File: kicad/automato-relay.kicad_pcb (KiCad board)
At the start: 2 copper layers, 39 parts, among them J1 TE-3-213598-4, J2 Screw_Terminal_01x03, J3 TE-3-213598-4, J4 Screw_Terminal_01x05, J5 TE-3-213598-4, J6 TE-3-213598-4, J7 Screw_Terminal_01x05, J8 TE-3-213598-4, K1 G5LE-14, K2 G5LE-14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

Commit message: Final Rev
Added varistor, poured power planes, added mounting holes, modified data headers, added space for IEC connector.
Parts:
- V1: footprint Varistor:RV_Disc_D7mm_W3.5mm_P5mm -> Varistor:RV_Disc_D15.5mm_W3.9mm_P7.5mm
- moved D10 4.00 mm to (160.0, 126.0)
- moved D11 4.00 mm to (220.0, 126.0)
- moved D12 4.00 mm to (280.0, 126.0)
- moved D9 4.00 mm to (100.0, 126.0)
- moved K1 4.00 mm to (98.0, 138.0)
- moved K2 4.00 mm to (158.0, 138.0)
- moved K3 4.00 mm to (218.0, 138.0)
- moved K4 4.00 mm to (278.0, 138.0)
- moved Q1 4.00 mm to (101.0, 121.0)
- moved Q2 4.00 mm to (161.0, 121.0)
- moved Q3 4.00 mm to (221.0, 121.0)
- moved Q4 4.00 mm to (281.0, 121.0)
- moved R2 4.00 mm to (157.0, 121.0)
- moved R4 4.00 mm to (217.0, 121.0)
- moved R5 4.00 mm to (97.0, 121.0)
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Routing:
- net 3V3: track 332.4 -> 65.6 mm, vias 6 -> 3
- net GND: track 542.1 -> 290.9 mm, vias 6 -> 7
- net ACL: track 316.9 -> 70.6 mm
- net ACE: track 312.2 -> 407.1 mm, vias 0 -> 10
- net Net-(C1-Pad1): track 23.2 -> 0.00 mm
- net Net-(C4-Pad1): track 23.2 -> 0.00 mm
- net Net-(C2-Pad1): track 22.6 -> 0.00 mm
- net Net-(C3-Pad1): track 22.2 -> 0.00 mm
- net LATCH: track 346.9 -> 345.1 mm
- net CTRL1: track 26.8 -> 28.5 mm
- net SDI: track 58.6 -> 57.1 mm
- net CTRL2: track 84.3 -> 85.4 mm
- net SDO: track 271.3 -> 270.4 mm
- net CTRL4: track 209.3 -> 210.1 mm
- net CTRL3: track 147.2 -> 147.9 mm
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- added copper zone on B.Cu, net 3V3
- added copper zone on B.Cu, net ACE
- added copper zone on F.Cu, net ACE
- added copper zone on B.Cu, net ACL
- added copper zone on B.Cu, net ACN
- added copper zone on B.Cu, net GND
- added copper zone on F.Cu, net Net-(C1-Pad1)
- added copper zone on F.Cu, net Net-(C2-Pad1)
- added copper zone on F.Cu, net Net-(C3-Pad1)
- added copper zone on F.Cu, net Net-(C4-Pad1)
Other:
- board outline added: 308 x 75 mm
- net class EARTH added: clearance 1, trace_width 0.25, via_dia 0.8, via_drill 0.4
- net class HV: trace_width 6 -> 8
- board text added: "Automato Relay v0.1"

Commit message: layout: remove vias on SDO
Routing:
- net SDO: track 270.4 -> 287.5 mm, vias 3 -> 1

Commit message: layout: add Earth pour on southern half of board (both sides)
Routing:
- net ACE: track 407.1 -> 444.9 mm, vias 10 -> 4
- net SDO: track 287.5 -> 286.7 mm
- net (no net): vias 4 -> 0

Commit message: layout: add GND and 3V3 pours on northern half of board
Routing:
- net GND: track 290.9 -> 71.9 mm, vias 7 -> 0
- net 3V3: track 65.6 -> 81.1 mm, vias 3 -> 1
- added copper zone on F.Cu, net GND
- removed copper zone on B.Cu, net GND
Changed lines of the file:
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@@
     (thickness 1.6)
     (drawings 7)
-    (tracks 263)
+    (tracks 240)
     (zones 0)
     (modules 39)
@@
   )
   (setup
-    (last_trace_width 3)
+    (last_trace_width 0.4572)
     (user_trace_width 0.3048)
     (user_trace_width 0.4572)
@@
   (segment (start 280 132) (end 280 127) (width 1) (layer F.Cu) (net 12))
   (segment (start 58 110.8) (end 58.2 110.6) (width 1) (layer F.Cu) (net 12))
-  (segment (start 58 121) (end 58 110.8) (width 5) (layer F.Cu) (net 12))
   (segment (start 100 127) (end 100 131.000024) (width 1) (layer F.Cu) (net 12))
-  (segment (start 100 132) (end 100 129) (width 1) (layer B.Cu) (net 12))
   (segment (start 160 132) (end 160 129) (width 1) (layer B.Cu) (net 12))
-  (segment (start 220 132) (end 220 129) (width 1) (layer B.Cu) (net 12))
-  (segment (start 58.2 121.2) (end 58 121) (width 1) (layer B.Cu) (net 12))
-  (segment (start 58.2 121.3) (end 58.2 121.2) (width 1) (layer B.Cu) (net 12))
-  (via (at 58.2 121.3) (size 1.5) (drill 1) (layers F.Cu B.Cu) (net 12))
-  (segment (start 58.2 128.2) (end 58.2 121.3) (width 5) (layer B.Cu) (net 12))
-  (segment (start 58.5 128.5) (end 58.2 128.2) (width 5) (layer B.Cu) (net 12))
-  (via (at 78.5 127.5) (size 0.8) (drill 0.4) (layers F.Cu B.Cu) (net 12))
-  (segment (start 77.87 127.5) (end 76.445 127.575) (width 0.6096) (layer F.Cu) (net 12))
-  (segment (start 78.5 127.5) (end 77.87 127.5) (width 0.6096) (layer F.Cu) (net 12))
-  (segment (start 277 129) (end 280 132) (width 1) (layer B.Cu) (net 12))
   (segment (start 68.825 128.45) (end 68.34239 128.93261) (width 0.4572) (layer F.Cu) (net 12))
   (segment (start 68.825 127.575) (end 68.825 128.45) (width 0.4572) (layer F.Cu) (net 12))
@@
   (via (at 66.000072 128.906179) (size 0.8) (drill 0.4) (layers F.Cu B.Cu) (net 12))
   (segment (start 66.026503 128.93261) (end 66.000072 128.906179) (width 0.4572) (layer F.Cu) (net 12))
-  (segment (start 280 132) (end 280 130) (width 1.5) (layer B.Cu) (net 12))
-  (segment (start 29.36 131.32) (end 30.68 130) (width 1) (layer B.Cu) (net 12))
   (segment (start 29 131.32) (end 29.36 131.32) (width 1) (layer B.Cu) (net 12))
+  (segment (start 73.575 131.32) (end 29 131.32) (width 0.4572) (layer F.Cu) (net 12))
+  (segment (start 76.445 128.45) (end 73.575 131.32) (width 0.4572) (layer F.Cu) (net 12))
+  (segment (start 76.445 127.575) (end 76.445 128.45) (width 0.4572) (layer F.Cu) (net 12))
   (segment (start 302 115) (end 313.24 126.24) (width 1) (layer B.Cu) (net 13))
   (segment (start 40 115) (end 302 115) (width 1) (layer B.Cu) (net 13))
@@
   (segment (start 70.517461 129.788789) (end 34.805989 129.788789) (width 0.4572) (layer F.Cu) (net 13))
   (segment (start 31.2572 126.24) (end 29 126.24) (width 0.4572) (layer F.Cu) (net 13))
+  (segment (start 71.5 130.5) (end 73.905 128.095) (width 0.4572) (layer F.Cu) (net 14))
+  (segment (start 32.254198 130.5) (end 71.5 130.5) (width 0.4572) (layer F.Cu) (net 14))
+  (segment (start 30.754198 129) (end 32.254198 130.5) (width 0.4572) (layer F.Cu) (net 14))
+  (segment (start 73.905 128.095) (end 73.905 127.575) (width 0.4572) (layer F.Cu) (net 14))
+  (segment (start 27.851174 129) (end 30.754198 129) (width 0.4572) (layer F.Cu) (net 14))
+  (segment (start 26.5 127.648826) (end 27.851174 129) (width 0.4572) (layer F.Cu) (net 14))
+  (segment (start 26.5 123.66) (end 26.5 127.648826) (width 0.4572) (layer F.Cu) (net 14))
   (segment (start 29 121.16) (end 26.5 123.66) (width 0.4572) (layer F.Cu) (net 14))
-  (segment (start 26.5 123.66) (end 26.5 126.797653) (width 0.4572) (layer F.Cu) (net 14))
-  (segment (start 29.754198 128) (end 32.254198 130.5) (width 0.4572) (layer F.Cu) (net 14))
-  (segment (start 26.5 126.797653) (end 27.702347 128) (width 0.4572) (layer F.Cu) (net 14))
-  (segment (start 27.702347 128) (end 29.754198 128) (width 0.4572) (layer F.Cu) (net 14))
-  (segment (start 32.254198 130.5) (end 71.5 130.5) (width 0.4572) (layer F.Cu) (net 14))
-  (segment (start 71.5 130.5) (end 73.905 128.095) (width 0.4572) (layer F.Cu) (net 14))
-  (segment (start 73.905 128.095) (end 73.905 127.575) (width 0.4572) (layer F.Cu) (net 14))
   (segment (start 29 116.08) (end 30.92 116.08) (width 1) (layer B.Cu) (net 15))
   (segment (start 316.24 113) (end 319 115.76) (width 1) (layer B.Cu) (net 15))
@@
   (segment (start 279.9625 121.9125) (end 280 121.95) (width 1) (layer F.Cu) (net 16))
   (segment (start 277 121.9125) (end 279.9625 121.9125) (width 1) (layer F.Cu) (net 16))
-  (via (at 214 123) (size 0.8) (drill 0.4) (layers F.Cu B.Cu) (net 16))
-  (segment (start 67.555 122.425) (end 67.555 120.555) (width 0.4572) (layer F.Cu) (net 16))
   (segment (start 318.68 111) (end 319 110.68) (width 1) (layer B.Cu) (net 16))
-  (segment (start 67 111) (end 318.68 111) (width 1) (layer B.Cu) (net 16))
   (segment (start 97 121.9125) (end 96.0875 121.9125) (width 1) (layer F.Cu) (net 16))
   (segment (start 96.0875 121.9125) (end 94.75 123.25) (width 1) (layer F.Cu) (net 16))
-  (via (at 274 123) (size 0.8) (drill 0.4) (layers F.Cu B.Cu) (net 16))
-  (via (at 94.75 123.25) (size 0.8) (drill 0.4) (layers F.Cu B.Cu) (net 16))
-  (segment (start 275.0875 121.9125) (end 274 123) (width 1) (layer F.Cu) (net 16))
-  (segment (start 277 121.9125) (end 275.0875 121.9125) (width 1) (layer F.Cu) (net 16))
-  (segment (start 215.0875 121.9125) (end 214 123) (width 1) (layer F.Cu) (net 16))
-  (segment (start 217 121.9125) (end 215.0875 121.9125) (width 1) (layer F.Cu) (net 16))
-  (via (at 154 123) (size 0.8) (drill 0.4) (layers F.Cu B.Cu) (net 16))
-  (segment (start 155.0875 121.9125) (end 157 121.9125) (width 1) (layer F.Cu) (net 16))
-  (segment (start 154 123) (end 155.0875 121.9125) (width 1) (layer F.Cu) (net 16))
-  (segment (start 72.635 125.135) (end 72.635 127.575) (width 0.6096) (layer F.Cu) (net 16))
-  (segment (start 67 109.5) (end 67 109.5) (width 2) (layer F.Cu) (net 16))
-  (via (at 67 109.5) (size 1.5) (drill 1) (layers F.Cu B.Cu) (net 16))
-  (segment (start 67.5 120) (end 67.5 120) (width 2) (layer F.Cu) (net 16))
-  (segment (start 67 110.5) (end 67 119) (width 5) (layer F.Cu) (net 16))
-  (via (at 67 119.5) (size 1.5) (drill 1) (layers F.Cu B.Cu) (net 16))
-  (segment (start 67 119) (end 67 119.000032) (width 2) (layer F.Cu) (net 16))
-  (via (at 72.5 124.5) (size 0.8) (drill 0.4) (layers F.Cu B.Cu) (net 16))
-  (segment (start 72.635 124.635) (end 72.5 124.5) (width 0.6096) (layer F.Cu) (net 16))
-  (segment (start 72.635 125.135) (end 72.635 124.635) (width 0.6096) (layer F.Cu) (net 16))
+  (segment (start 32 114) (end 29 111) (width 0.4572) (layer F.Cu) (net 16))
+  (segment (start 32 119) (end 32 114) (width 0.4572) (layer F.Cu) (net 16))
+  (segment (start 38 125) (end 32 119) (width 0.4572) (layer F.Cu) (net 16))
+  (segment (start 64.98 125) (end 38 125) (width 0.4572) (layer F.Cu) (net 16))
+  (segment (start 67.555 122.425) (end 64.98 125) (width 0.4572) (layer F.Cu) (net 16))
+  (segment (start 67.555 123.3) (end 67.555 122.425) (width 0.4572) (layer F.Cu) (net 16))
+  (segment (start 69.255 125) (end 67.555 123.3) (width 0.4572) (layer F.Cu) (net 16))
+  (segment (start 70.935 125) (end 69.255 125) (width 0.4572) (layer F.Cu) (net 16))
+  (segment (start 72.635 126.7) (end 70.935 125) (width 0.4572) (layer F.Cu) (net 16))
+  (segment (start 72.635 127.575) (end 72.635 126.7) (width 0.4572) (layer F.Cu) (net 16))
   (segment (start 64.425 127.575) (end 67.555 127.575) (width 0.4572) (layer F.Cu) (net 17))
   (segment (start 64 127) (end 64.425 127.575) (width 0.4572) (layer F.Cu) (net 17))
@@
     )
   )
-  (zone (net 16) (net_name GND) (layer B.Cu) (hatch edge 0.508)
-    (connect_pads yes (clearance 0.5))
-    (min_thickness 0.254)
-    (fill yes (arc_segments 32) (thermal_gap 0.508) (thermal_bridge_width 0.508) (smoothing fillet) (radius 2))
-    (polygon
-      (pts
-        (xy 321 125) (xy 27 125) (xy 27 107) (xy 321 107)
-      )
-    )
-  )
-  (zone (net 12) (net_name 3V3) (layer B.Cu) (hatch edge 0.508)
-    (connect_pads yes (clearance 0.75))
-    (min_thickness 0.254)
-    (fill yes (arc_segments 32) (thermal_gap 0.508) (thermal_bridge_width 0.508) (smoothing fillet) (radius 2))
-    (polygon
-      (pts
-        (xy 280.5 131) (xy 27 131) (xy 27 127) (xy 280.5 127)
-      )
-    )
-  )
   (zone (net 10) (net_name ACE) (layer F.Cu) (hatch edge 0.508)
     (connect_pads yes (clearance 0))
@@
       )
     )
+  )
+  (zone (net 16) (net_name GND) (layer F.Cu) (hatch edge 0.508)
+    (priority 1)
+    (connect_pads yes (clearance 0))
+    (min_thickness 0.254)
+    (fill yes (arc_segments 32) (thermal_gap 0.508) (thermal_bridge_width 0.508) (smoothing fillet) (radius 2))
+    (polygon
+      (pts
+        (xy 328 134) (xy 20 134) (xy 20 97) (xy 328 97)
+      )
+    )
+  )
+  (zone (net 12) (net_name 3V3) (layer B.Cu) (hatch edge 0.508)
+    (priority 1)
+    (connect_pads yes (clearance 0))
+    (min_thickness 0.254)
+    (fill yes (arc_segments 32) (thermal_gap 0.508) (thermal_bridge_width 0.508) (smoothing fillet) (radius 2))
+    (polygon
+      (pts
+        (xy 328 134) (xy 20 134) (xy 20 97) (xy 328 97)
+      )
+    )

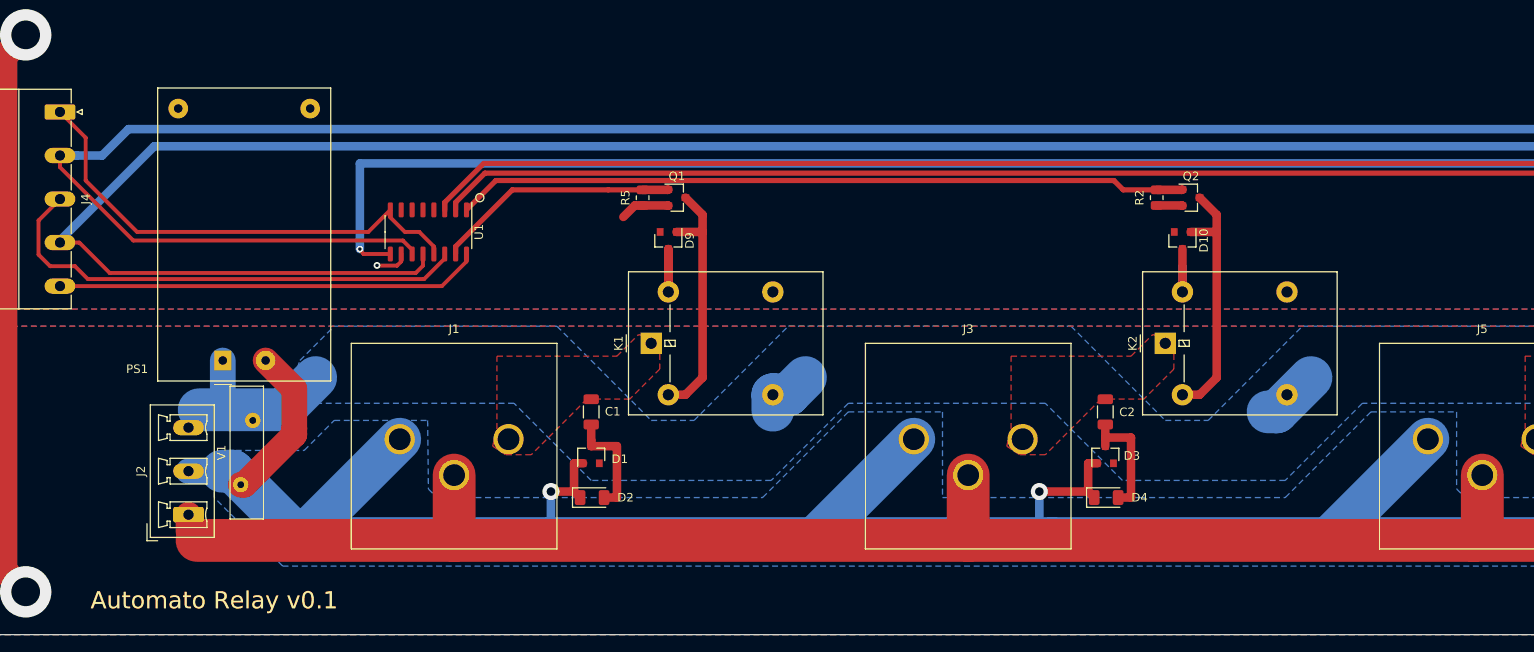
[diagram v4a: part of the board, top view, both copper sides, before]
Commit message: layout: modify and move revision label
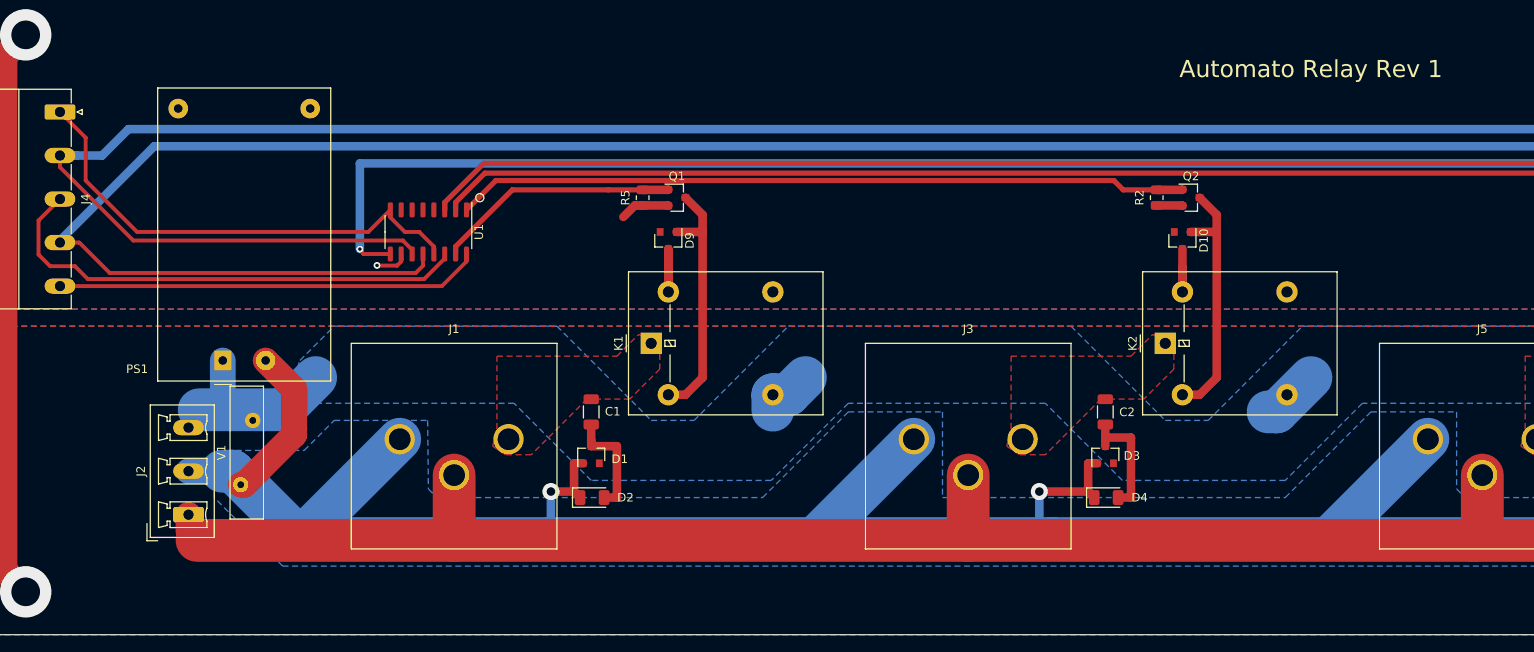
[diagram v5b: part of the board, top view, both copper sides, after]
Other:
- board text added: "Automato Relay Rev 1"
- board text removed: "Automato Relay v0.1"
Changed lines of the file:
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@@
   (general
     (thickness 1.6)
-    (drawings 7)
+    (drawings 6)
     (tracks 240)
     (zones 0)
@@
     )
   )
-  (gr_text "Automato Relay v0.1" (at 47 168) (layer F.SilkS)
+  (gr_text "Automato Relay Rev 1" (at 175 106) (layer F.SilkS)
     (effects (font (size 2 2) (thickness 0.3)))
   )
-  (gr_text "Automato Relay v0.1" (at 47 168) (layer F.Cu)
-    (effects (font (size 2 2) (thickness 0.5)))
-  )
   (gr_circle (center 78 121) (end 78.319867 120.64414) (layer F.SilkS) (width 0.12))

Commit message: layout: replace mounting holes with proper M3 pads, add rounded corners
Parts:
- added REF**: MountingHole_3.2mm_M3_Pad, MountingHole:MountingHole_3.2mm_M3_Pad, F.Cu at (323.0, 167.0)
- added REF**: MountingHole_3.2mm_M3_Pad, MountingHole:MountingHole_3.2mm_M3_Pad, F.Cu at (25.0, 102.0)
- added REF**: MountingHole_3.2mm_M3_Pad, MountingHole:MountingHole_3.2mm_M3_Pad, F.Cu at (25.0, 167.0)
- added REF**: MountingHole_3.2mm_M3_Pad, MountingHole:MountingHole_3.2mm_M3_Pad, F.Cu at (323.0, 102.0)
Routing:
- net ACE: track 444.9 -> 445.5 mm, vias 4 -> 0
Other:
- outline, holes or cut-outs redrawn

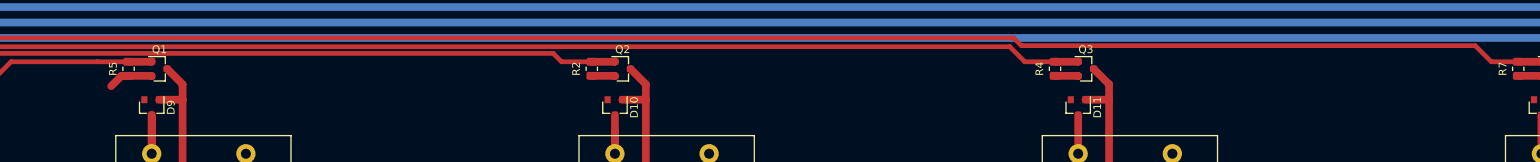
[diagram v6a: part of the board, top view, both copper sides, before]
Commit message: add testpoints for CTRL1,2,3,4
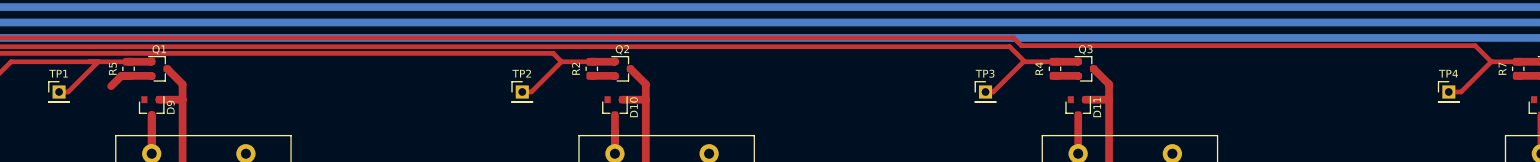
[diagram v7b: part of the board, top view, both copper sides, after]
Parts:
- added TP1: TestPoint, Connector_PinHeader_2.54mm:PinHeader_1x01_P2.54mm_Vertical, F.Cu at (88.0, 124.0)
- added TP2: TestPoint, Connector_PinHeader_2.54mm:PinHeader_1x01_P2.54mm_Vertical, F.Cu at (148.0, 124.0)
- added TP3: TestPoint, Connector_PinHeader_2.54mm:PinHeader_1x01_P2.54mm_Vertical, F.Cu at (208.0, 124.0)
- added TP4: TestPoint, Connector_PinHeader_2.54mm:PinHeader_1x01_P2.54mm_Vertical, F.Cu at (268.0, 124.0)
- C1, C2, C3, C4: value 100n -> 47n
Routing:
- net CTRL1: track 28.5 -> 36.3 mm
- net CTRL4: track 210.1 -> 217.3 mm
- net CTRL2: track 85.4 -> 92.1 mm
- net CTRL3: track 147.9 -> 154.6 mm
